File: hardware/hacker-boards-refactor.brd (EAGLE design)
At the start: 27.6 x 58.4 mm, 38 parts, among them J1 MICRO_USB_B_JST_MC5BR3-M404-4S

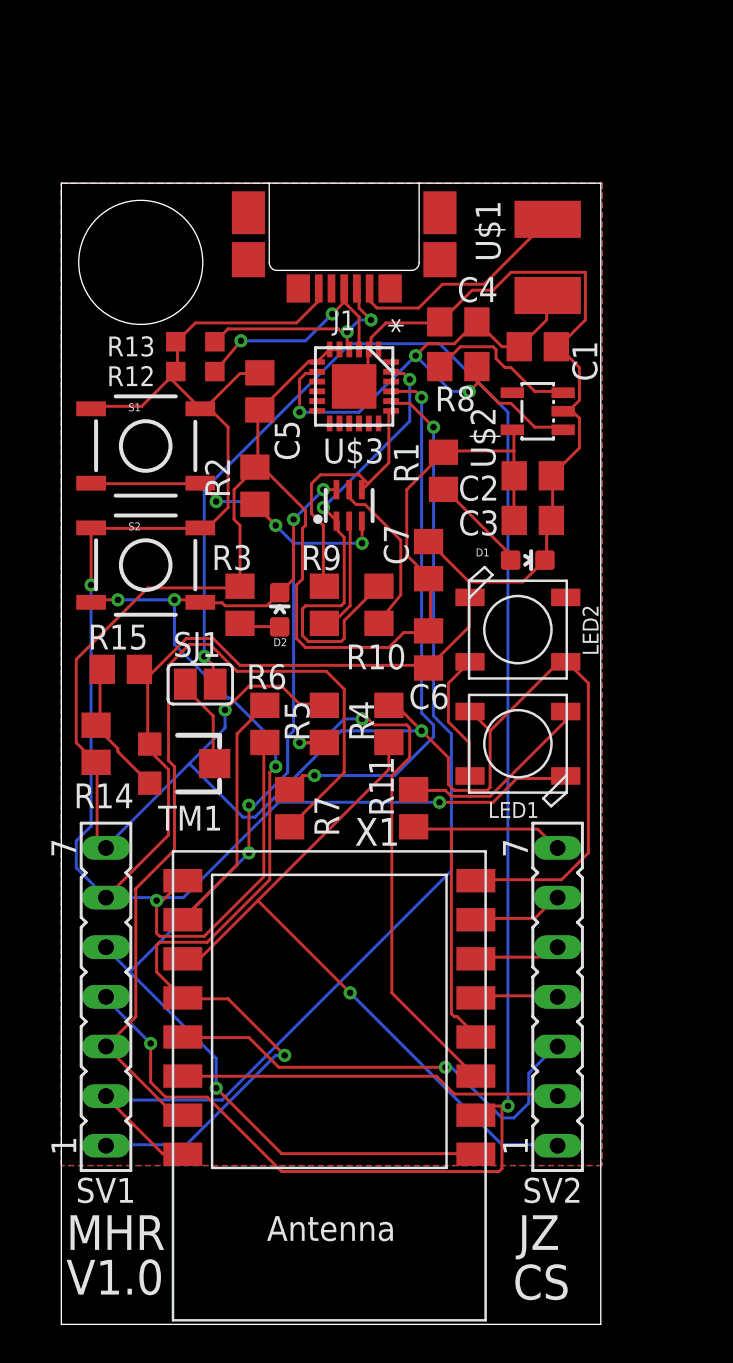
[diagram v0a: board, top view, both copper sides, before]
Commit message: Added header labels, fixed silk, cleared space for extra ESP-12 pads
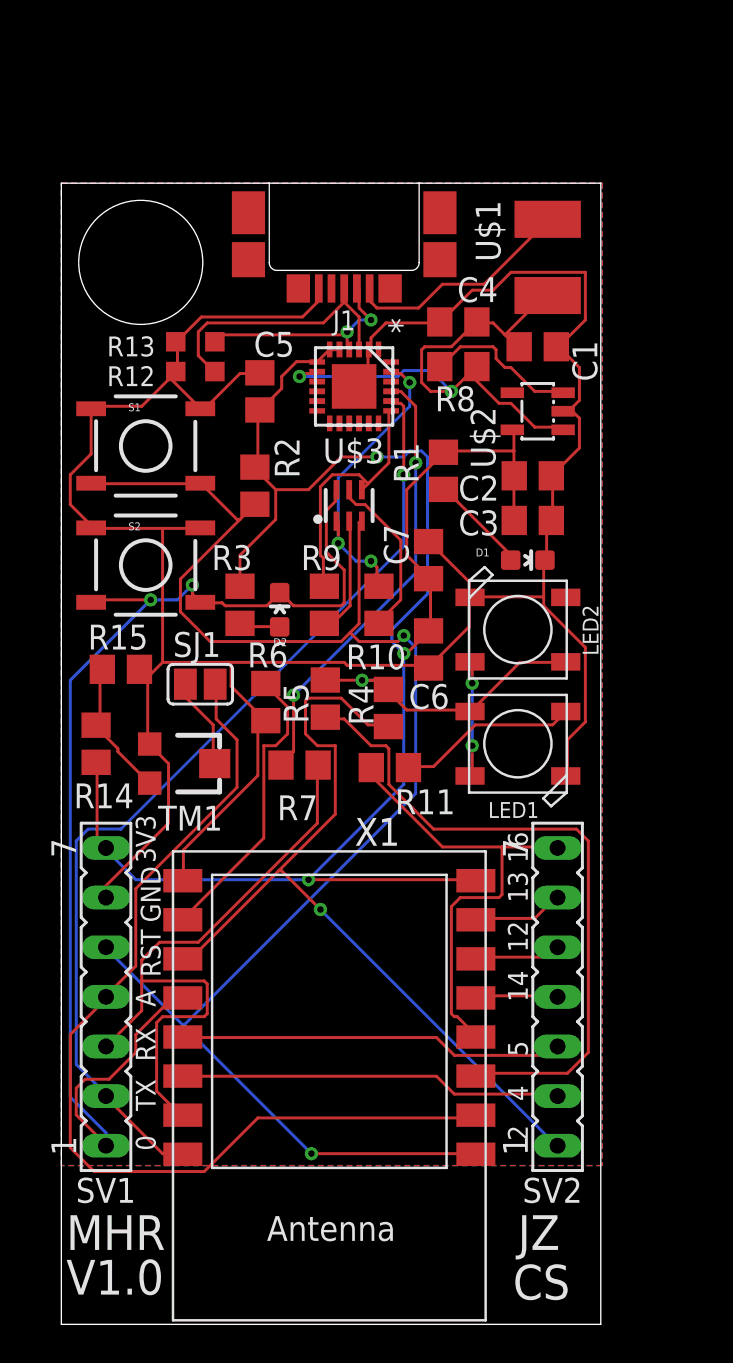
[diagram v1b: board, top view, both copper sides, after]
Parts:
- moved R11 2.41 mm to (16.8, 21.1), turned to 180 degrees
- moved R7 2.27 mm to (12.2, 21.3), turned to 0 degrees
- moved R5 1.30 mm to (13.5, 24.7)
- moved R6 1.12 mm to (10.5, 24.5)
- moved R4 0.81 mm to (16.7, 24.2)
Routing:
- net ANALOG_IN: track 96.1 -> 50.2 mm, vias 3 -> 0
- net GND: track 174.8 -> 142.0 mm, vias 3 -> 0
- net +3V3: track 136.6 -> 110.5 mm, vias 2 -> 4
- net RST: track 67.7 -> 82.5 mm, vias 6 -> 2
- net RX: track 45.1 -> 33.1 mm
- net DTR: track 24.2 -> 15.6 mm, vias 2 -> 3
- net CH_PD: track 27.6 -> 34.3 mm, vias 2 -> 0
- net GPIO2: track 36.5 -> 42.8 mm
- net USB_RX: track 27.8 -> 22.8 mm
- net GPIO16: track 19.0 -> 24.0 mm
- net TX: track 53.7 -> 49.8 mm
- net GPIO5/SCL: track 23.3 -> 19.8 mm, vias 1 -> 0
- net GPIO15: track 12.7 -> 15.1 mm
- net USB+: track 11.7 -> 14.0 mm, vias 2 -> 0
- net GPIO0: track 61.7 -> 63.0 mm, vias 6 -> 2
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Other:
- board text added: "0"
- board text added: "12"
- board text added: "13"
- board text added: "14"
- board text added: "16"
- board text added: "2"
- board text added: "3V3"
- board text added: "4"
- board text added: "5"
- board text added: "A"
- board text added: "GND"
- board text added: "RST"
- board text added: "RX"
- board text added: "TX"

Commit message: Slightly enlarged board for new headers, extensively tweaked silkscreen
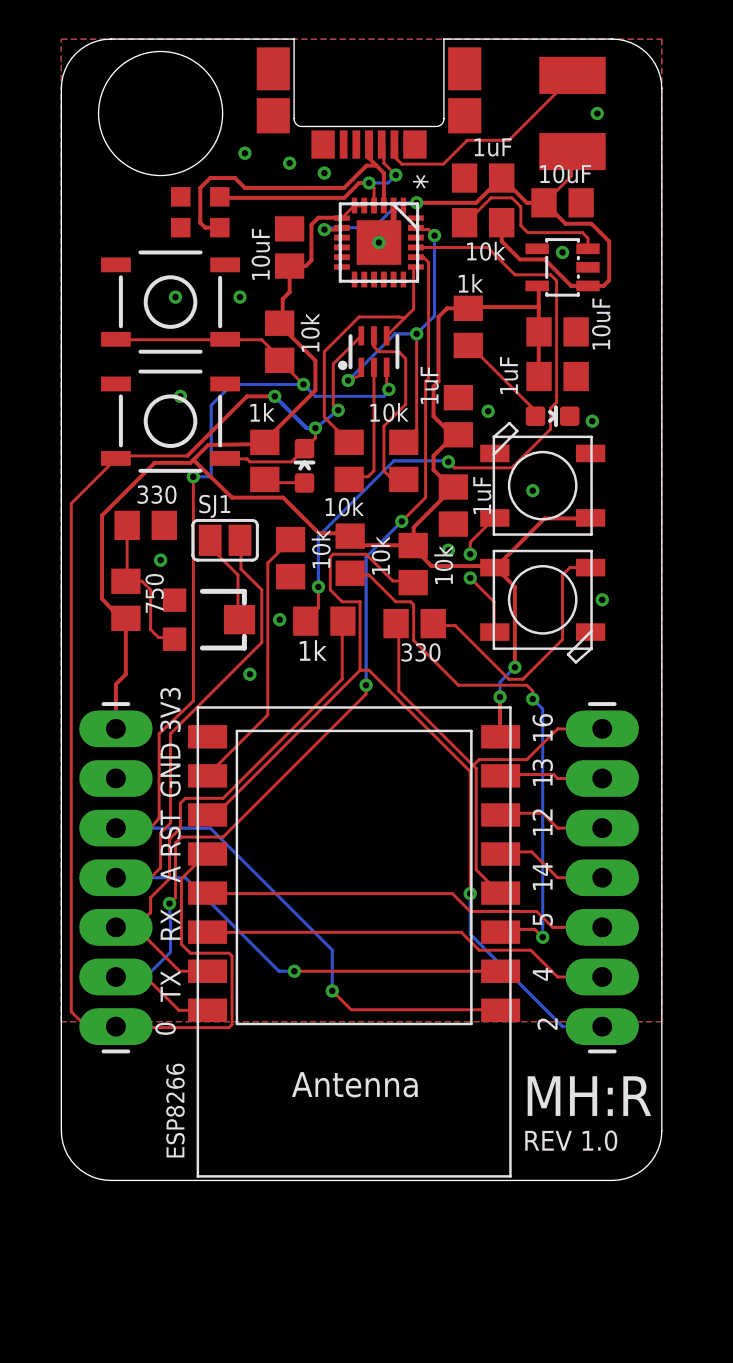
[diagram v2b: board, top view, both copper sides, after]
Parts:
- removed SV1, SV2: (no value), con-lsta:FE07
- added JP1, JP2: (no value), hacker-board:1X07_LONGPADS
- moved U$4 7.98 mm to (16.0, 42.4)
- moved C7 7.52 mm to (20.3, 39.1)
- moved C5 7.52 mm to (11.7, 47.8)
- moved R14 7.52 mm to (3.30, 29.7)
- moved C3 7.47 mm to (25.4, 41.1)
- moved LED2 7.47 mm to (24.6, 35.6)
- moved R5 7.47 mm to (14.8, 32.0)
- moved R7 7.47 mm to (13.5, 28.6)
- moved S2 7.47 mm to (5.59, 38.9)
- moved TM1 7.47 mm to (7.62, 28.7)
- moved X1 7.47 mm to (15.0, 13.2)
- moved C1 7.47 mm to (25.7, 50.0)
- moved C2 7.47 mm to (25.4, 43.4)
- moved C4 7.47 mm to (21.6, 51.3)
- moved D1 7.47 mm to (25.1, 39.1)
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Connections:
- net +3V3: now also JP1.7; no longer SV1.7
- net ANALOG_IN: now also JP1.4; no longer SV1.4
- net GND: now also JP1.6; no longer SV1.6
- net GPIO0: now also JP1.1; no longer SV1.1
- net GPIO12: now also JP2.3; no longer SV2.5
- net GPIO13: now also JP2.2; no longer SV2.6
- net GPIO14: now also JP2.4; no longer SV2.4
- net GPIO16: now also JP2.1; no longer SV2.7
- net GPIO2: now also JP2.7; no longer SV2.1
- net GPIO4/SDA: now also JP2.6; no longer SV2.2
- net GPIO5/SCL: now also JP2.5; no longer SV2.3
- net RST: now also JP1.5; no longer SV1.5
- net RX: now also JP1.3; no longer SV1.3
- net TX: now also JP1.2; no longer SV1.2
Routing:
- net GND: track 142.0 -> 2.32 mm, vias 0 -> 17
- net +3V3: track 110.5 -> 97.0 mm, vias 4 -> 2
- net USB_RX: track 22.8 -> 34.7 mm
- net RST: track 82.5 -> 71.9 mm, vias 2 -> 4
- net GPIO0: track 63.0 -> 73.6 mm, vias 2 -> 3
- net ANALOG_IN: track 50.2 -> 43.6 mm, vias 0 -> 1
- net CH_PD: track 34.3 -> 28.1 mm, vias 0 -> 2
- net RX: track 33.1 -> 27.2 mm
- net GPIO2: track 42.8 -> 47.6 mm
- net N$6: track 9.24 -> 13.6 mm
- net DTR: track 15.6 -> 17.9 mm
- net USB+: track 14.0 -> 16.3 mm
- net TX: track 49.8 -> 51.5 mm, vias 1 -> 3
- net GPIO14: track 4.24 -> 5.79 mm
- net GPIO4/SDA: track 19.6 -> 21.1 mm
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- added copper zone on layer 1, net GND
- added copper zone on layer 16, net GND
- removed copper zone on layer 16, net N$10
- removed copper zone on layer 1, net N$9
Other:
- board size 27.6 x 58.4 mm -> 30.7 x 58.4 mm
- board text added: "ESP8266"
- board text added: "Jonathan Zarger Colin Szechy"
- board text added: "MH:R"
- board text added: "MHACKS: REFACTOR HACKER BOARD"
- board text added: "PLACE NFC HERE"
- board text added: "REV 1.0"
- board text removed: "CS"
- board text removed: "JZ"
- board text removed: "MHR"
- board text removed: "V1.0"
